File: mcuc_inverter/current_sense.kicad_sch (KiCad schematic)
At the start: 30 parts, among them J501 HOYS U harness - JST PA B05B-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, J502 HOYS V harness - JST PA B05B-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, J503 HOYS W harness - JST PA B05B-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, U501 HOYS 200-S/SP33, U502 HOYS 200-S/SP33, U503 HOYS 200-S/SP33, U504 TLV7032/LM2903-class open-dra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, U505 TLV7032/LM2903-class open-dra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, U506 TLV7032/LM2903-class open-dra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

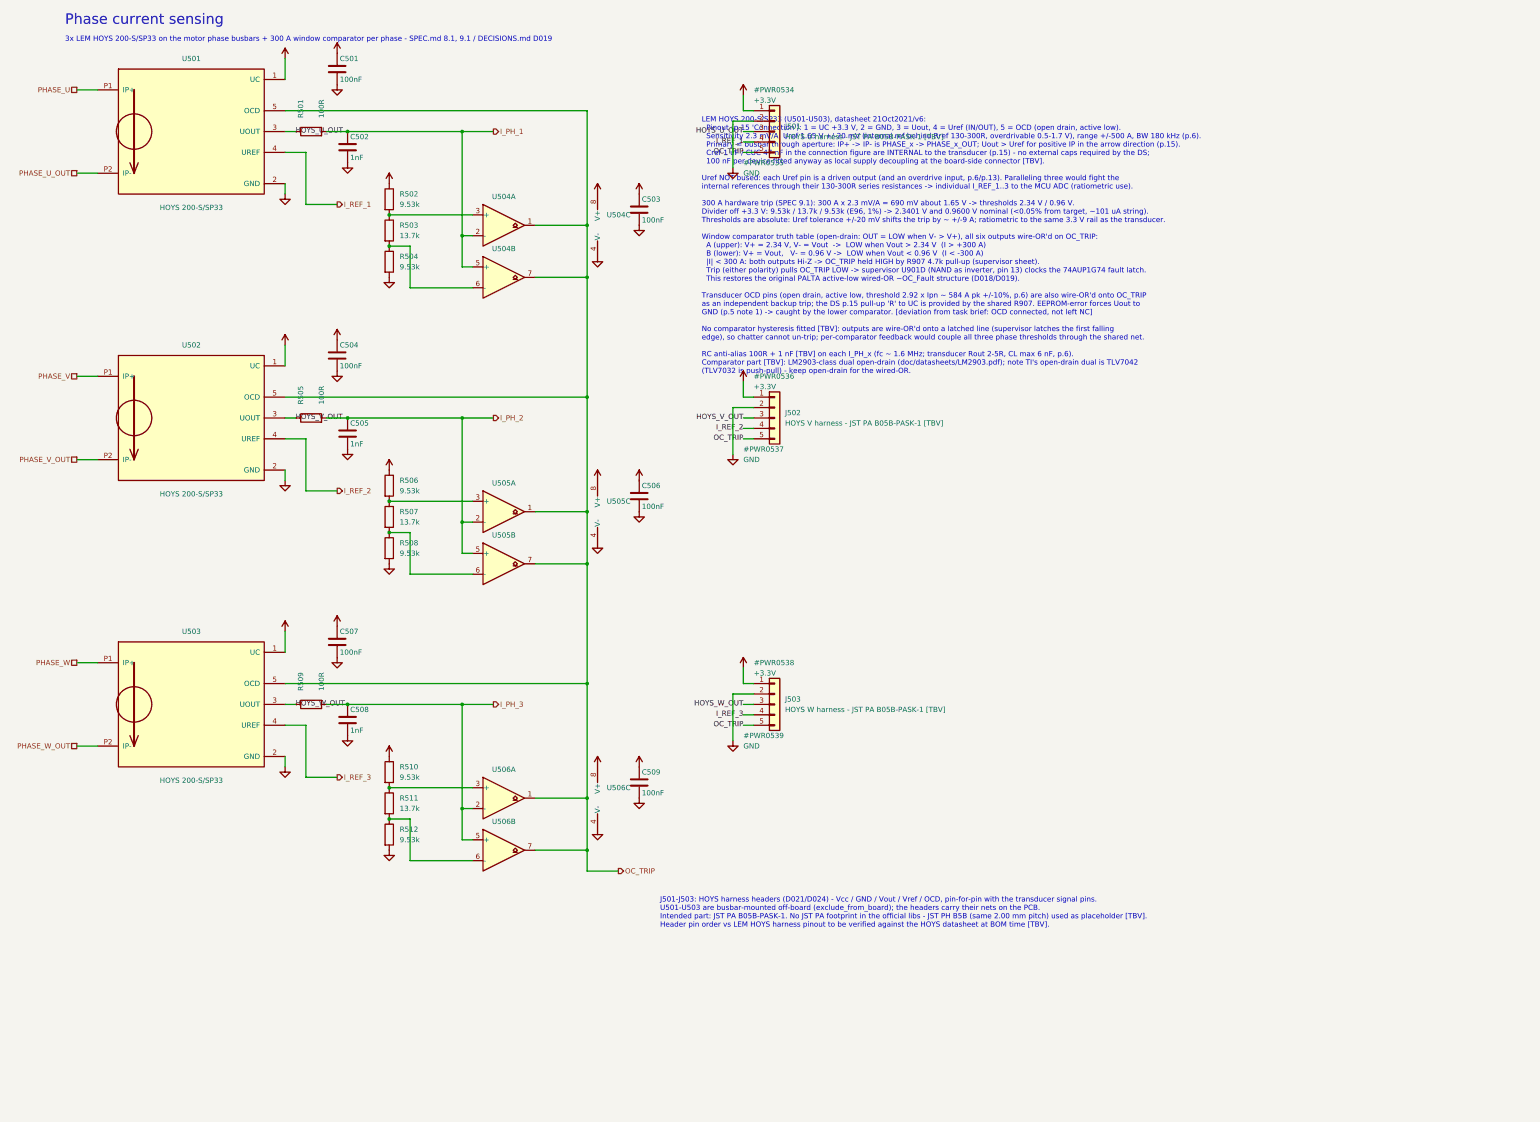
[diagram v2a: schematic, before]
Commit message: Fix precharge, current sense, position, comms per review
Also repairs a library-breaking defect the agent found while working:
the VOM1271T symbol contained a raw newline inside a quoted string,
which silently truncated mcuc_inverter.kicad_sym at parse - every
symbol defined after it was unresolvable. That had been latent since
the symbol was written.

MJ-2/3 - the comparators were wrong twice over: TLV7032 is push-pull
(six of them wire-ORed together plus three open-drain transducer OCD
pins is direct contention), and LM2903's input common-mode range on
3.3 V stops at 1.8 V, below the 2.34 V upper threshold, so the
over-current half could never trip. Now TLV7022DDFR: true open-drain,
rail-to-rail input, 260 ns instead of ~3 us.

MJ-4 - the trip point was really 245-356 A because the thresholds
rode a +-4% rail while the transducer's reference is absolute. Each
phase's window is now servo'd off its own Uref through an OPA376
buffer, so the threshold tracks the sensor: 300 A +-8 A.

MJ-7 - a harness disconnect was not fail-safe: that phase's OCD left
the wire-OR and the input floated. 100k pull-downs make an open
harness read as a large negative current and latch the trip at
power-up, before HV is applied.

MJ-12 - the active discharge can no longer be commanded into a live
bus: SN74LVC1G97 computes DISCHARGE_EN AND NOT(CONTACTOR_EN)
self-contained on the sheet, plus a 10k boot pull-down.

Discharge gate now has a real Miller clamp (BSS138 + 1n + 10k) firing
at V_GS ~1.34 V, below the FET's 1.8 V threshold, in under 15 ns -
the 450 V dv/dt step could previously inject ~4.4 V against a 10M
pull-down and a uA-class photovoltaic turn-off.

Bleeder 18.7k -> 14k (56 k total, 56.4 s to 60 V, meeting the <60 s
requirement it was failing at 75.4 s). Precharge resistor respec'd to
>=65 J. Coil freewheels upsized to ES1G/ES2G with anti-series SMBJ24A
TVS for fast relay release, which forced the coil drivers to 60 V
parts - documented with a 17% margin note.

Position: SinCos f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
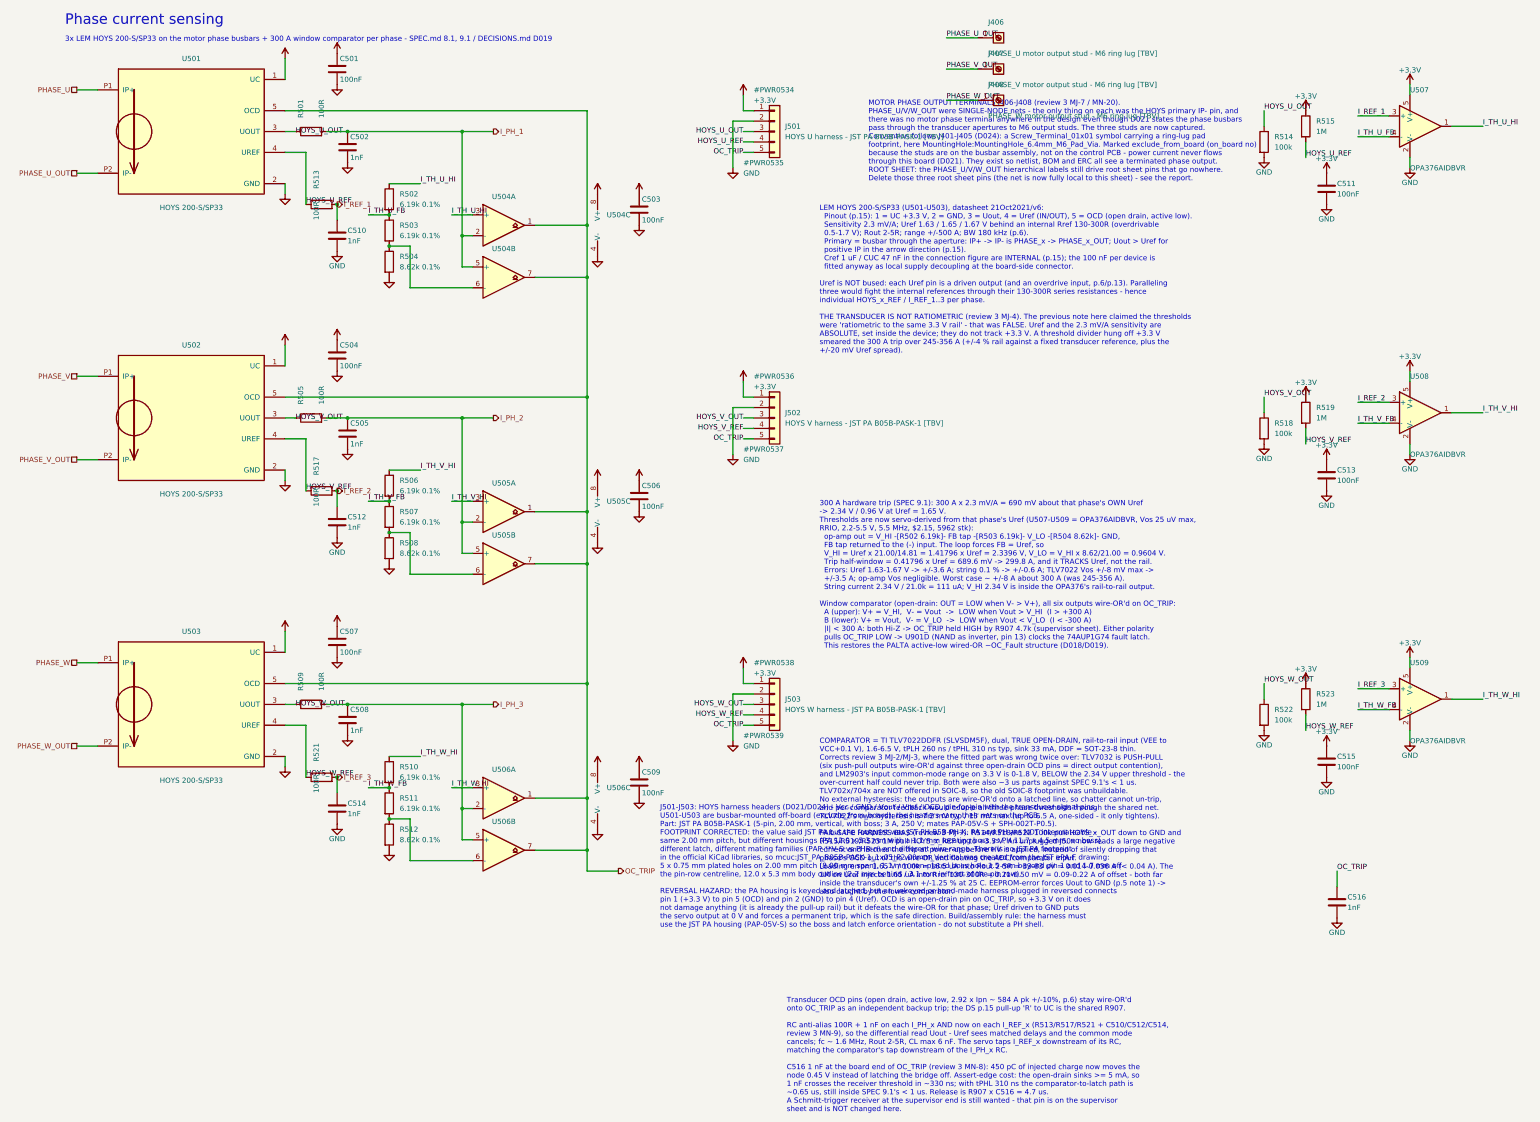
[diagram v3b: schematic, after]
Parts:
- added C510, C512, C514, C516: 1nF, Capacitor_SMD:C_0603_1608Metric, symbol Device:C
- added C511, C513, C515: 100nF, Capacitor_SMD:C_0603_1608Metric, symbol Device:C
- added J406: PHASE_U motor output stud - M6 ring lug [TBV], MountingHole:MountingHole_6.4mm_M6_Pad_Via, symbol Connector:Screw_Terminal_01x01
- added J407: PHASE_V motor output stud - M6 ring lug [TBV], MountingHole:MountingHole_6.4mm_M6_Pad_Via, symbol Connector:Screw_Terminal_01x01
- added J408: PHASE_W motor output stud - M6 ring lug [TBV], MountingHole:MountingHole_6.4mm_M6_Pad_Via, symbol Connector:Screw_Terminal_01x01
- added R513, R517, R521: 100R, Resistor_SMD:R_0603_1608Metric, symbol Device:R
- added R514, R518, R522: 100k, Resistor_SMD:R_0603_1608Metric, symbol Device:R
- added R515, R519, R523: 1M, Resistor_SMD:R_0603_1608Metric, symbol Device:R
- added U507, U508, U509: OPA376AIDBVR, Package_TO_SOT_SMD:SOT-23-5, symbol mcuc:OPA376AIDBVR
- J501, J502, J503: footprint Connector_JST:JST_PH_B5B-PH-K_1x05_P2.00mm_Vertical -> mcuc:JST_PA_B05B-PASK-1_1x05_P2.00mm_Vertical
- R502, R506, R510: value 9.53k -> 6.19k 0.1%
- R503, R507, R511: value 13.7k -> 6.19k 0.1%
- R504, R508, R512: value 9.53k -> 8.62k 0.1%
- U504, U505, U506: value TLV7032/LM2903-class open-drain [TBV] -> TLV7022DDFR; footprint Package_SO:SOIC-8_3.9x4.9mm_P1.27mm -> Package_TO_SOT_SMD:Texas_DDF0008A_SOT-8_1.6x2.9mm_P0.65mm; symbol Comparator:LM2903 -> mcuc:TLV7022DDF
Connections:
- net +3.3V: now also C511.1, C513.1, C515.1, R515.1, R519.1, R523.1, U507.5 (V+), U508.5 (V+), U509.5 (V+); no longer R502.1, R506.1, R510.1
- net GND: now also C510.2, C511.2, C512.2, C513.2, C514.2, C515.2, C516.2, R514.2, R518.2, R522.2, U507.2 (V-), U508.2 (V-), U509.2 (V-)
- net HOYS_U_OUT: now also R514.1
- net HOYS_V_OUT: now also R518.1
- net HOYS_W_OUT: now also R522.1
- net I_REF_1: now also C510.1, R513.2, U507.3 (+); no longer J501.4 (Pin_4), U501.4 (UREF)
- net I_REF_2: now also C512.1, R517.2, U508.3 (+); no longer J502.4 (Pin_4), U502.4 (UREF)
- net I_REF_3: now also C514.1, R521.2, U509.3 (+); no longer J503.4 (Pin_4), U503.4 (UREF)
- net OC_TRIP: now also C516.1
- net PHASE_U_OUT: now also J406.1 (Pin_1)
- net PHASE_V_OUT: now also J407.1 (Pin_1)
- net PHASE_W_OUT: now also J408.1 (Pin_1)
- net I_TH_V_FB: now reaches R506.2, R507.1
- net I_TH_V_FB: now also U508.4 (-); no longer U505.3 (+)
- net I_TH_U_FB: now reaches R502.2, R503.1
- net I_TH_U_FB: now also U507.4 (-); no longer U504.3 (+)
- net I_TH_W_FB: now reaches R510.2, R511.1
- net I_TH_W_FB: now also U509.4 (-); no longer U506.3 (+)
- new net HOYS_U_REF: J501.4 (Pin_4), R513.1, R515.2, U501.4 (UREF)
- new net HOYS_V_REF: J502.4 (Pin_4), R517.1, R519.2, U502.4 (UREF)
- new net HOYS_W_REF: J503.4 (Pin_4), R521.1, R523.2, U503.4 (UREF)
- new net I_TH_U_HI: R502.1, U504.3 (+), U507.1
- new net I_TH_V_HI: R506.1, U505.3 (+), U508.1
- new net I_TH_W_HI: R510.1, U506.3 (+), U509.1
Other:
- note added: "300 A hardware trip (SPEC 9.1): 300 A x 2.3 mV/A = 690 mV about that phase's OWN Uref -> 2.34 V / 0.96 V at Uref = 1.65 V. Thresholds are now servo-derived from that phase's Uref (U507-U509 = OPA376AIDBVR, Vos 25 uV max, RRIO, 2.2-5.5 V, 5.5 MHz, $2.15, 5962 stk): op-amp out = V_HI -[R502 6.19k]- FB tap -[R503 6.19k]- V_LO -[R504 8.62k]- GND, FB tap returned to the (-) input. The loop forces FB =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"
- note added: "COMPARATOR = TI TLV7022DDFR (SLVSDM5F), dual, TRUE OPEN-DRAIN, rail-to-rail input (VEE to VCC+0.1 V), 1.6-6.5 V, tPLH 260 ns / tPHL 310 ns typ, sink 33 mA, DDF = SOT-23-8 thin. Corrects review 3 MJ-2/MJ-3, where the fitted part was wrong twice over: TLV7032 is PUSH-PULL (six push-pull outputs wire-OR'd against three open-drain OCD pins = direct output contention), and LM2903's input common-mode r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"
- note added: "J501-J503: HOYS harness headers (D021/D024) - Vcc / GND / Vout / Vref / OCD, pin-for-pin with the transducer signal pins. U501-U503 are busbar-mounted off-board (exclude_from_board); the headers carry their nets on the PCB. Part: JST PA B05B-PASK-1 (5-pin, 2.00 mm, vertical, with boss; 3 A, 250 V; mates PAP-05V-S + SPH-002T-P0.5). FOOTPRINT CORRECTED: the value said JST PA but the footprint was J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"
- note added: "LEM HOYS 200-S/SP33 (U501-U503), datasheet 21Oct2021/v6: Pinout (p.15): 1 = UC +3.3 V, 2 = GND, 3 = Uout, 4 = Uref (IN/OUT), 5 = OCD (open drain, active low). Sensitivity 2.3 mV/A; Uref 1.63 / 1.65 / 1.67 V behind an internal Rref 130-300R (overdrivable 0.5-1.7 V); Rout 2-5R; range +/-500 A; BW 180 kHz (p.6). Primary = busbar through the aperture: IP+ -> IP- is PHASE_x -> PHASE_x_OUT; Uout > Uref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"
- note added: "MOTOR PHASE OUTPUT TERMINALS J406-J408 (review 3 MJ-7 / MN-20). PHASE_U/V/W_OUT were SINGLE-NODE nets - the only thing on each was the HOYS primary IP- pin, and there was no motor phase terminal anywhere in the design even though D021 states the phase busbars pass through the transducer apertures to M6 output studs. The three studs are now captured. Convention follows J401-J405 (D024): a Screw_Te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"
- note added: "Transducer OCD pins (open drain, active low, 2.92 x Ipn ~ 584 A pk +/-10%, p.6) stay wire-OR'd onto OC_TRIP as an independent backup trip; the DS p.15 pull-up 'R' to UC is the shared R907. RC anti-alias 100R + 1 nF on each I_PH_x AND now on each I_REF_x (R513/R517/R521 + C510/C512/C514, review 3 MN-9), so the differential read Uout - Uref sees matched delays and the common mode cancels; fc ~ 1.6 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"
- note removed: "J501-J503: HOYS harness headers (D021/D024) - Vcc / GND / Vout / Vref / OCD, pin-for-pin with the transducer signal pins. U501-U503 are busbar-mounted off-board (exclude_from_board); the headers carry their nets on the PCB. Intended part: JST PA B05B-PASK-1. No JST PA footprint in the official libs - JST PH B5B (same 2.00 mm pitch) used as placeholder [TBV]. Header pin order vs LEM HOYS harness p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"
- note removed: "LEM HOYS 200-S/SP33 (U501-U503), datasheet 21Oct2021/v6: Pinout (p.15 'Connection'): 1 = UC +3.3 V, 2 = GND, 3 = Uout, 4 = Uref (IN/OUT), 5 = OCD (open drain, active low). Sensitivity 2.3 mV/A, Uref 1.65 V +/-20 mV (internal ref behind Rref 130-300R, overdrivable 0.5-1.7 V), range +/-500 A, BW 180 kHz (p.6). Primary = busbar through aperture: IP+ -> IP- is PHASE_x -> PHASE_x_OUT; Uout > Uref for 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"
